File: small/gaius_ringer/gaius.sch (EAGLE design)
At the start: 30 parts, among them Q1 2N5088, Q2 2N3906-, Q3 2N5088

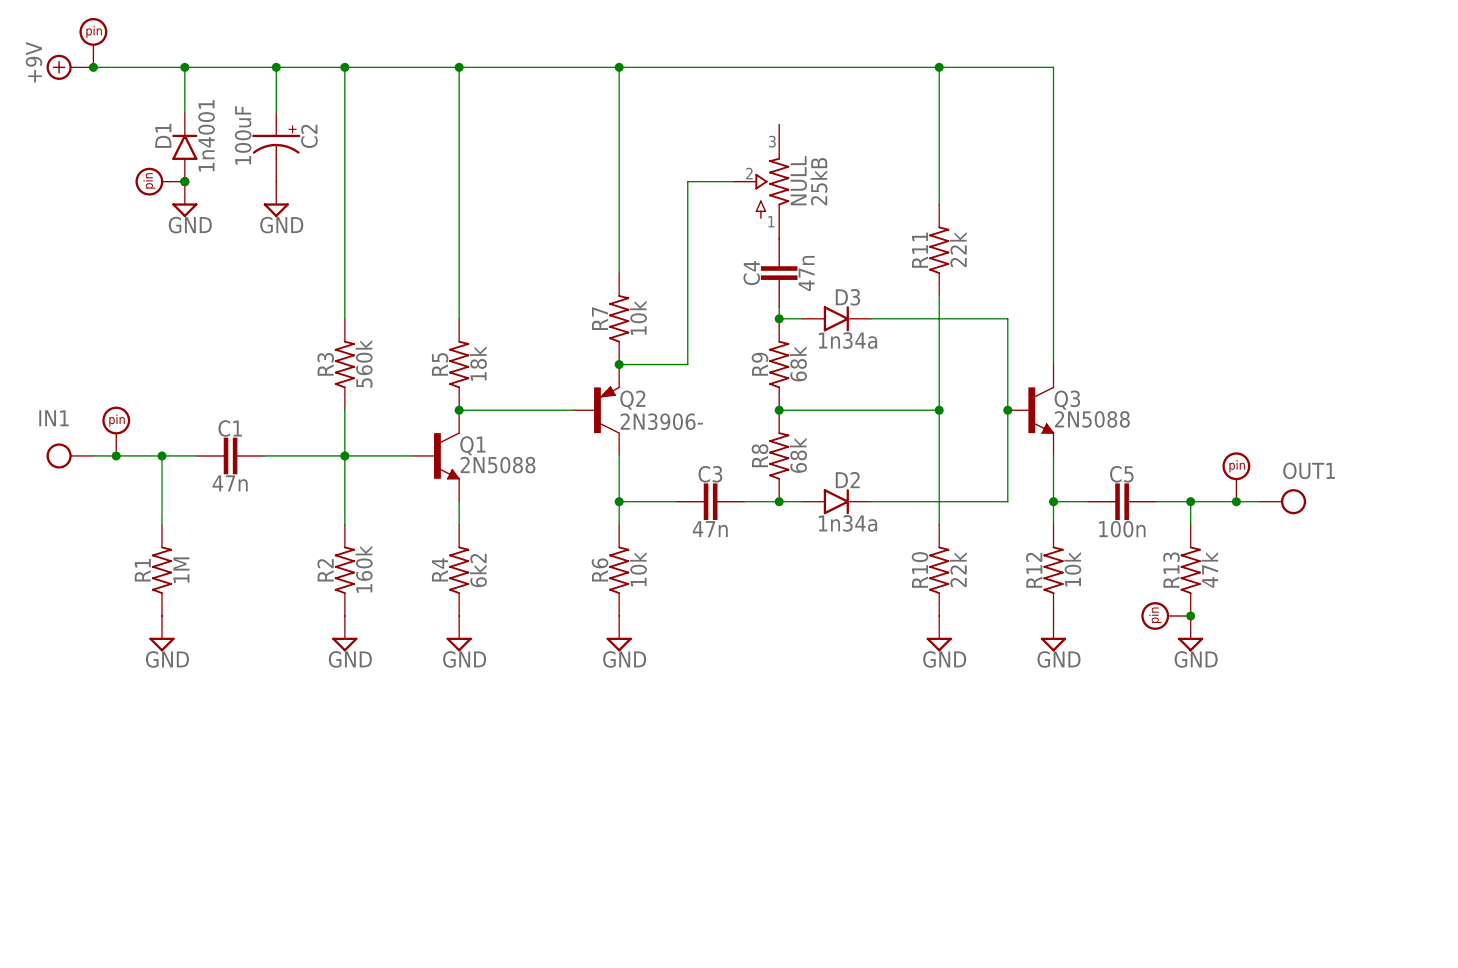
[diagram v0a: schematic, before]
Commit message: updated Gaius Ringer & Janus Drive, added Chimera Chorus
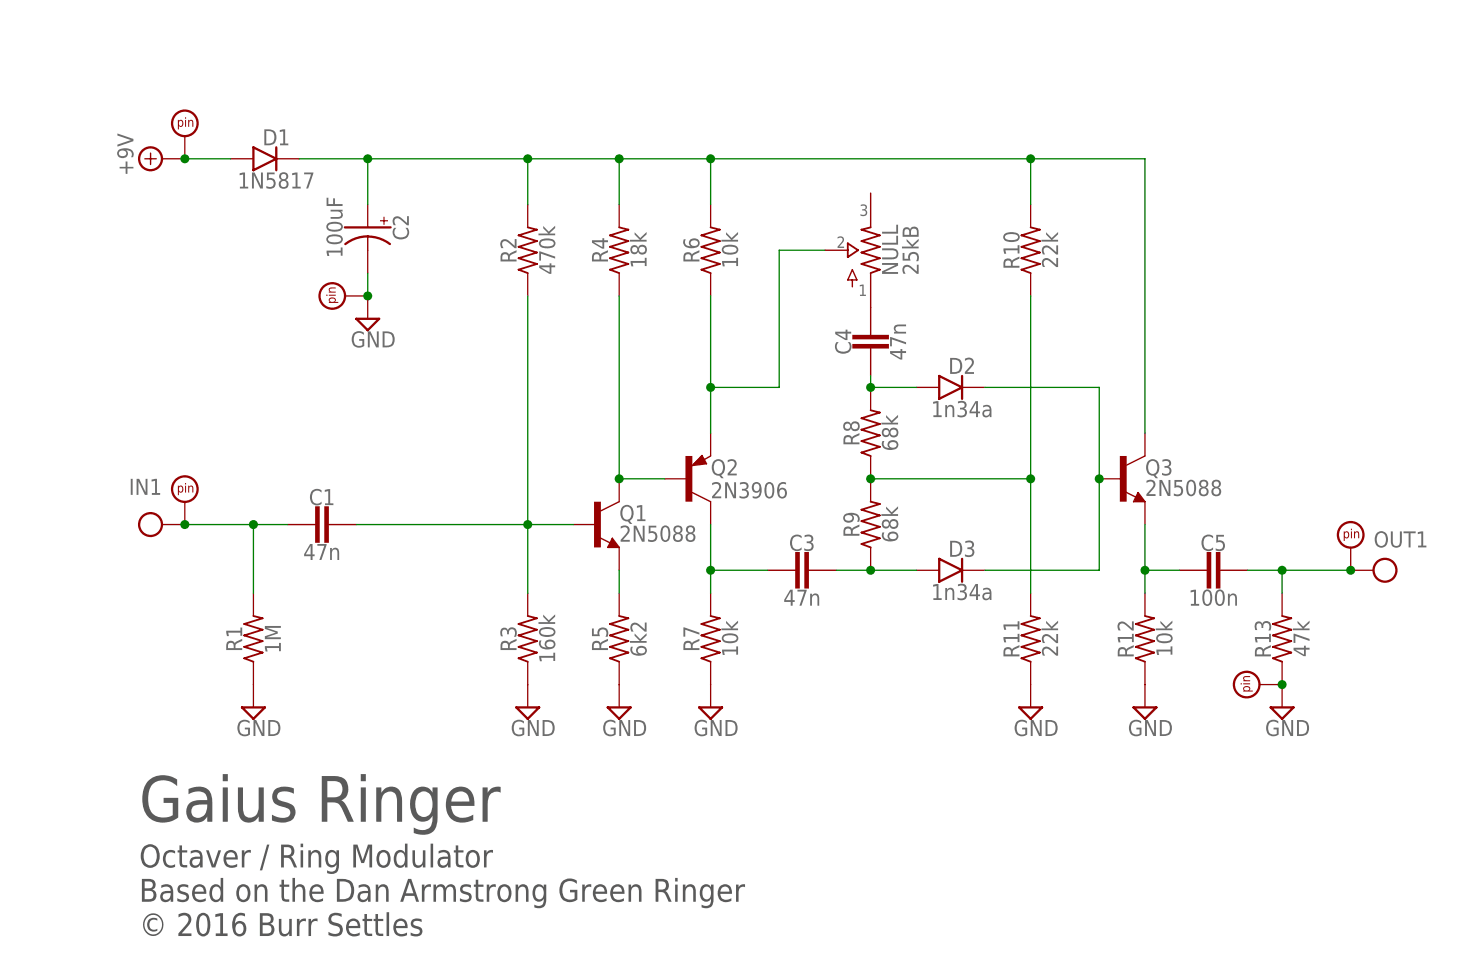
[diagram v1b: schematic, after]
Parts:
- C5: device capacitors-film:CER/FILMBOX.2 -> capacitors-film:CER/FILMBOX.1
- D1: value 1n4001 -> 1N5817
- NULL: device potentiometers:POTSSMALL_PADS -> potentiometers:POTSTRIM
- Q2: value 2N3906- -> 2N3906
- R2: value 160k -> 470k
- R3: value 560k -> 160k
- R4: value 6k2 -> 18k
- R5: value 18k -> 6k2
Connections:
- new net N$12: C2.+, D1.C, Q3.C, R10.2, R2.2, R4.2, R6.2
- net +9V: now also D1.A; no longer C2.+, D1.C, Q3.C, R11.2, R3.2, R5.2, R7.2
- net GND: now also R11.1, R3.1, R5.1, R7.1; no longer D1.A, R10.1, R2.1, R4.1, R6.1
- net N$1: now also R4.1; no longer R5.1
- net N$2: now also R5.2; no longer R4.2
- net N$3: now also R2.1, R3.2; no longer R2.2, R3.1
- net N$4: now also D2.A, R8.2; no longer D3.A, R9.2
- net N$5: now also R6.1; no longer R7.1
- net N$6: now also R10.1, R11.2, R8.1, R9.2; no longer R10.2, R11.1, R8.2, R9.1
- net N$8: now also R7.2; no longer R6.2
- net N$9: now also D3.A, R9.1; no longer D2.A, R8.1
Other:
- note added: "Gaius Ringer"
- note added: "Octaver / Ring Modulator Based on the Dan Armstrong Green Ringer © 2016 Burr Settles"
- moved on the sheet: C1, C2, C3, C4, C5, D1, D2, D3, NULL, Q1, Q2, Q3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

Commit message: updates to a few small pedals
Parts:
- C2: value 100uF -> 100u
- D2, D3: value 1n34a -> 1N34A
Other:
- note added: "GAIUS RINGER"
- note added: "OCTAVER / RING MODULATOR based on the Dan Armstrong Green Ringer © 2016 burr settles"
- note removed: "Gaius Ringer"
- note removed: "Octaver / Ring Modulator Based on the Dan Armstrong Green Ringer © 2016 Burr Settles"
- moved on the sheet: C1, C2, C3, C4, C5, D2, D3, NULL, Q1, Q2, Q3, R1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

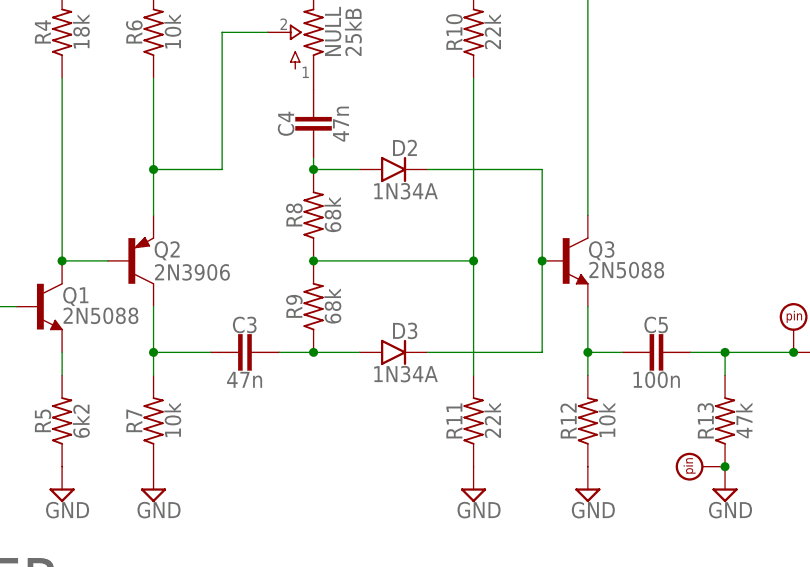
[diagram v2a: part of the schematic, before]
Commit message: added phaser schematic; minor board tweaks
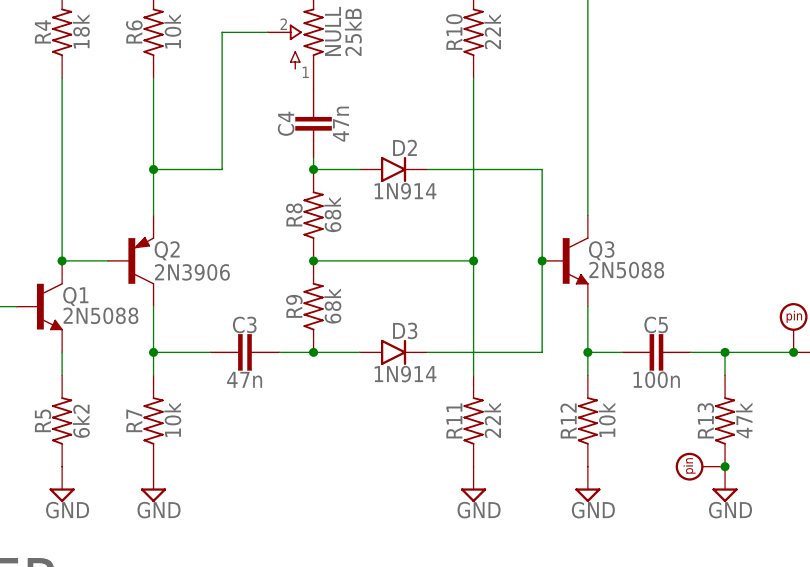
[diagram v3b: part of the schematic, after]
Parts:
- D2, D3: value 1N34A -> 1N914
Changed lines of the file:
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@@
 <part name="R9" library="resistors" deviceset="R_" device=".3B" value="68k"/>
 <part name="R8" library="resistors" deviceset="R_" device=".3B" value="68k"/>
-<part name="D2" library="diodes" deviceset="DO35" device=".2" value="1N34A"/>
-<part name="D3" library="diodes" deviceset="DO35" device=".2" value="1N34A"/>
+<part name="D2" library="diodes" deviceset="DO35" device=".2" value="1N914"/>
+<part name="D3" library="diodes" deviceset="DO35" device=".2" value="1N914"/>
 <part name="Q3" library="transistors" deviceset="2N5088" device=""/>
 <part name="Q2" library="transistors" deviceset="2N3906" device="-" value="2N3906"/>

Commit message: formatting updates
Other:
- note added: "OCTAVER / RING MODULATOR based on the dan armstrong green ringer (c) 2016 burr settles"
- note removed: "OCTAVER / RING MODULATOR based on the Dan Armstrong Green Ringer © 2016 burr settles"
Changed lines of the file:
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@@
 <sheet>
 <plain>
-<text x="2.54" y="15.24" size="5.08" layer="97">GAIUS RINGER</text>
-<text x="2.54" y="2.54" size="2.54" layer="97">OCTAVER / RING MODULATOR
-based on the Dan Armstrong Green Ringer
-© 2016 burr settles</text>
+<text x="2.54" y="12.7" size="6.4516" layer="97">GAIUS RINGER</text>
+<text x="2.54" y="2.54" size="1.9304" layer="97">OCTAVER / RING MODULATOR
+based on the dan armstrong green ringer
+(c) 2016 burr settles</text>
 </plain>
 <instances>
